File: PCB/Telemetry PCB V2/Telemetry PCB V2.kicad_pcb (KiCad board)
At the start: 4 copper layers, 70 x 70 mm, 50 parts, among them IC1 E22-900M22S, J1 USB_C_Receptacle_USB2.0_16P, J2 DBG/PGRM Hdr., J3 DATA IN, J4 GPS, J5 Batt, SW1 SW_MEC_5E, SW2 SW_MEC_5E, U1 STM32F411CEUx, U2 MCP1700x-250xxTT, U3 AP62200WU, Y1 25MHZ 20pF, Y2 32.768k 12.5pF

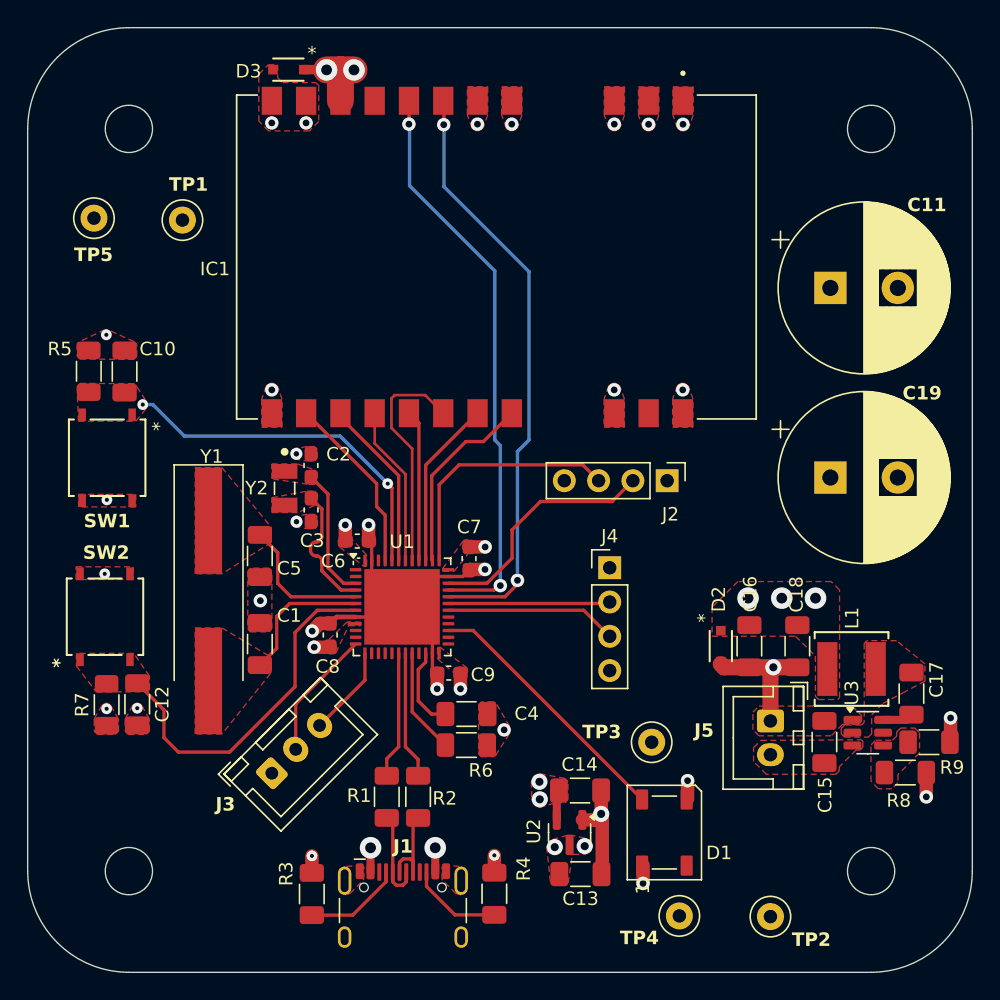
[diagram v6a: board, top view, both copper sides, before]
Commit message: :D
board is done as best I can tell

This update fully removed the smoothing caps as experienced people don't believe they are necessary. This resulted in moving a couple components around.

The vias greater than 0.5mm have had solder mask free zones added on them to prevent JLC from trying plug them because JLC says that plugging is likely to fail on large vias.
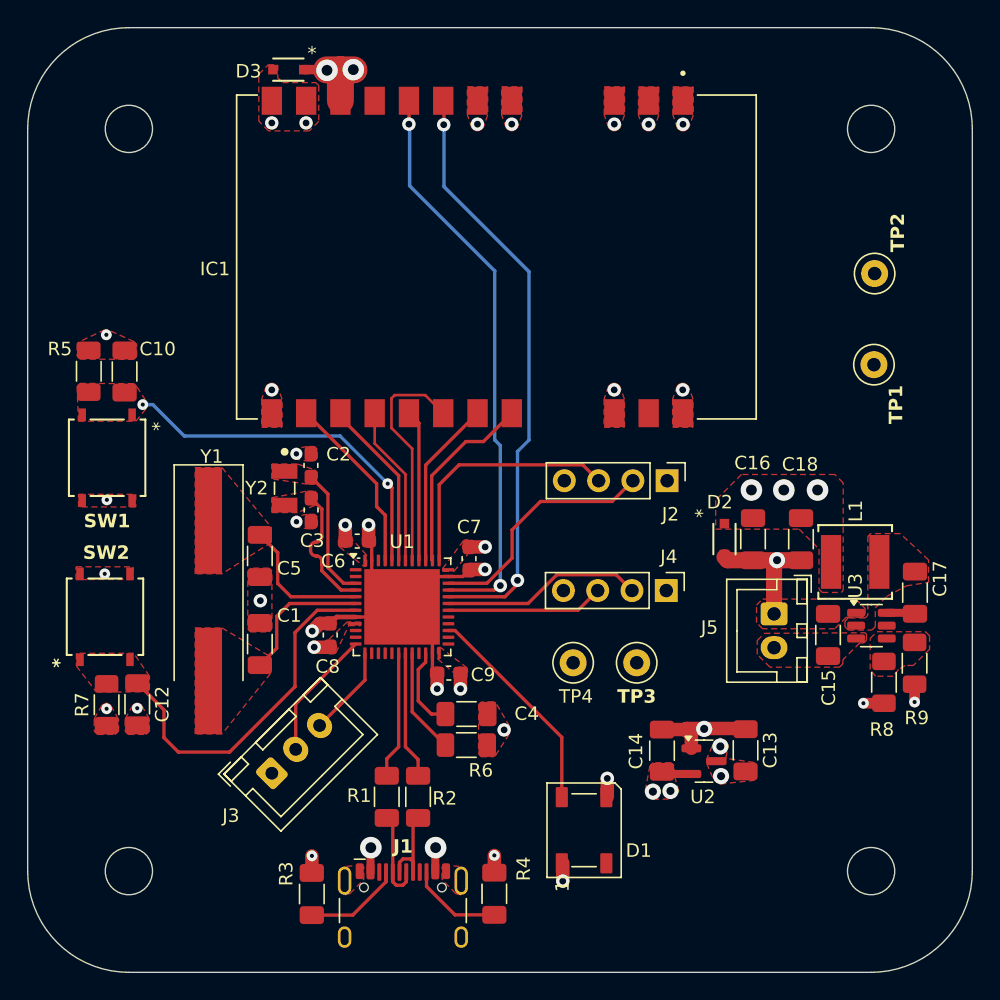
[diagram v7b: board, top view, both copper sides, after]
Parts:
- removed C11, C19: 1000uF, Capacitor_THT:CP_Radial_D12.5mm_P5.00mm
- removed the TP1 at (134.3, 62.7)
- removed TP5: TestPoint, TestPoint:TestPoint_Loop_D1.80mm_Drill1.0mm_Beaded
- added TP4: TestPoint, TestPoint:TestPoint_Loop_D1.80mm_Drill1.0mm_Beaded, F.Cu at (163.3, 95.5)
- J5: value Batt -> Battery
- moved TP2 48.3 mm to (185.6, 66.7), turned to 90 degrees
- moved TP1 43.3 mm to (185.6, 73.4), turned to 90 degrees
- moved C13 15.3 mm to (176.1, 102.0), turned to 90 degrees
- moved U2 11.3 mm to (173.0, 102.8), turned to 0 degrees
- moved C15 7.94 mm to (182.2, 93.4)
- moved C16 7.94 mm to (176.6, 86.3)
- moved C18 7.94 mm to (180.2, 86.3)
- moved L1 7.94 mm to (184.2, 88.0)
- moved U3 7.94 mm to (185.4, 92.7)
- moved D2 7.94 mm to (174.5, 86.3)
- moved J5 7.94 mm to (178.2, 91.9)
- moved C17 7.48 mm to (188.6, 90.3)
- moved R8 6.87 mm to (186.3, 97.0), turned to -90 degrees
- moved C14 6.75 mm to (169.9, 102.0), turned to 90 degrees
- moved TP3 5.99 mm to (168.0, 95.5)
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- renumbered TP4 to TP1
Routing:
- net DIN: track 19.5 -> 16.1 mm
- net RX: track 12.0 -> 15.0 mm
- net TX: track 12.7 -> 11.7 mm
- net +5V: track 13.0 -> 12.4 mm

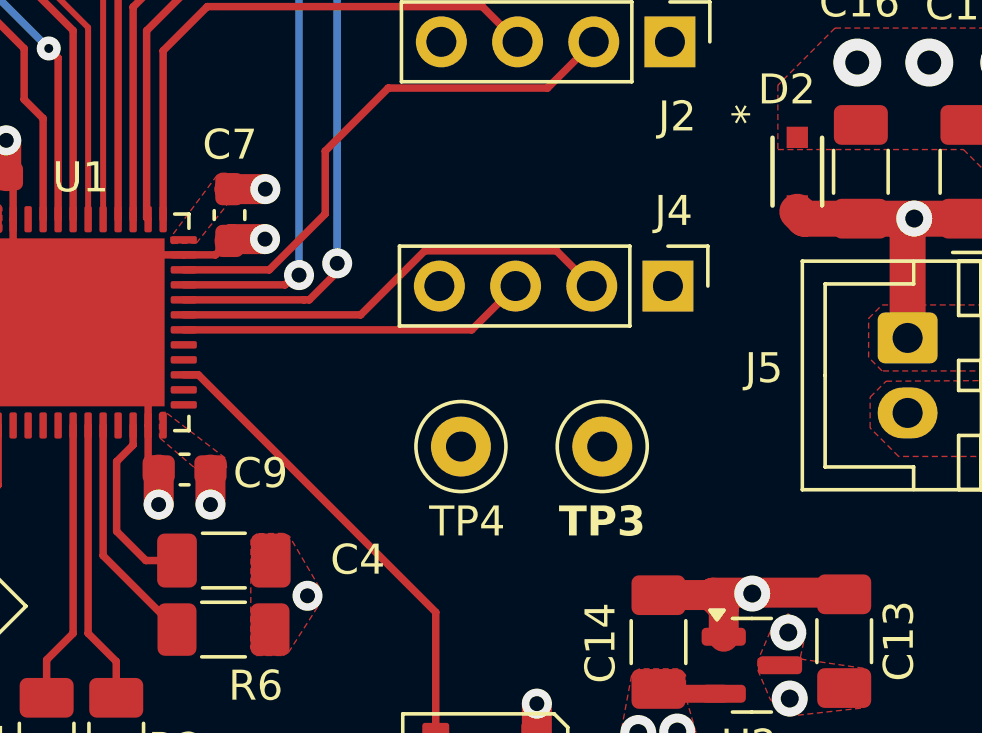
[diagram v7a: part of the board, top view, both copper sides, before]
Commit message: Changed GPS power to 5V
Changed GPS power to 5V because I was not sure what it's current draw is and we don't have a ton of spare capacity on the 3.3V power regulator. Powering of of 5V is also likely more power efficient as it is not passing through a linear voltage regulator
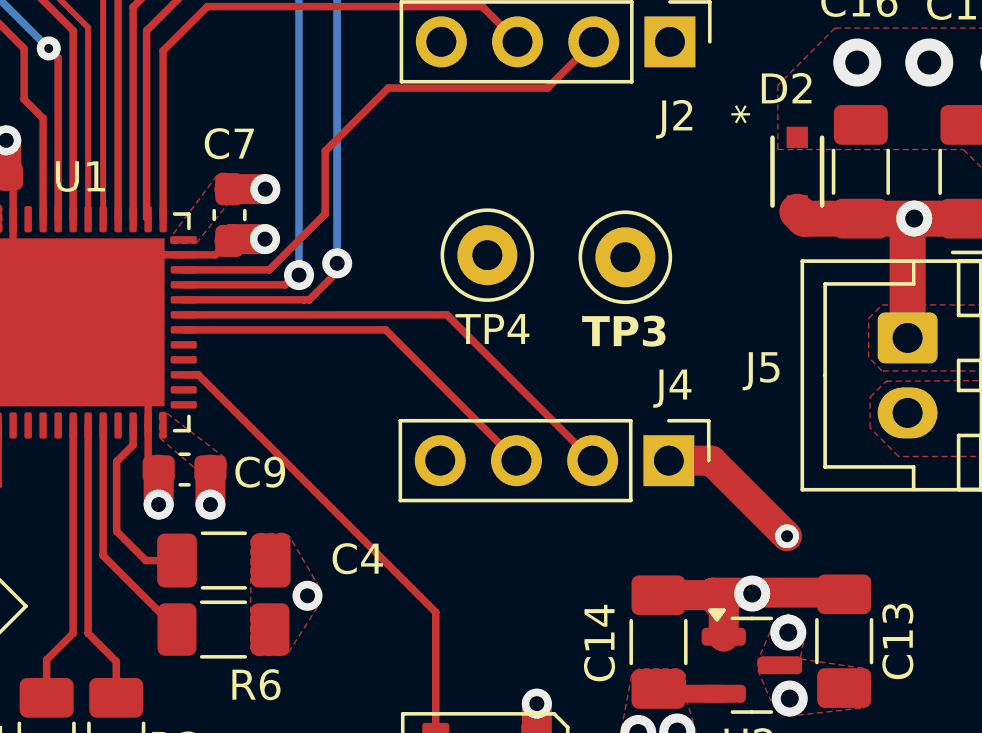
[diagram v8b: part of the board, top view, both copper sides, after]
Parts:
- Y1: value 25MHZ 20pF -> 25MHZ 18pF
- moved TP4 6.44 mm to (164.2, 89.1)
- moved TP3 6.36 mm to (168.8, 89.2)
- moved J4 5.82 mm to (170.2, 96.0)
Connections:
- J4 pad 1: +3.3V -> +5V
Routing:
- net +5V: track 12.4 -> 17.4 mm, vias 11 -> 12
- net TX: track 11.7 -> 12.9 mm
- net RX: track 15.0 -> 15.6 mm
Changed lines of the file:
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@@
 	(footprint "TestPoint:TestPoint_Loop_D1.80mm_Drill1.0mm_Beaded"
 		(layer "F.Cu")
-		(at 168 95.5)
+		(at 168.77 89.19)
 		(descr "wire loop with bead as test point, loop diameter 1.8mm, hole diameter 1.0mm")
 		(tags "test point wire loop bead")
@@
 		(tags "SMD SMT crystal hand-soldering")
 		(property "Reference" "Y1"
-			(at -10.692499 -0.235 180)
+			(at -10.692499 -0.235 360)
 			(layer "F.SilkS")
 			(effects
@@
 			)
 		)
-		(property "Value" "25MHZ 20pF"
+		(property "Value" "25MHZ 18pF"
 			(at -4.322499 3.335 90)
 			(layer "F.Fab")
@@
 	(footprint "Connector_PinHeader_2.54mm:PinHeader_1x04_P2.54mm_Vertical"
 		(layer "F.Cu")
-		(at 170.19 90.15 -90)
+		(at 170.22 95.97 -90)
 		(descr "Through hole straight pin header, 1x04, 2.54mm pitch, single row")
 		(tags "Through hole pin header THT 1x04 2.54mm single row")
@@
 			(layers "*.Cu" "*.Mask")
 			(remove_unused_layers no)
-			(net 7 "+3.3V")
+			(net 10 "+5V")
 			(pinfunction "Pin_1")
 			(pintype "passive")
@@
 	(footprint "TestPoint:TestPoint_Loop_D1.80mm_Drill1.0mm_Beaded"
 		(layer "F.Cu")
-		(at 163.29 95.5)
+		(at 164.17 89.12)
 		(descr "wire loop with bead as test point, loop diameter 1.8mm, hole diameter 1.0mm")
 		(tags "test point wire loop bead")
@@
 	)
 	(segment
+		(start 171.64 95.97)
+		(end 174.16 98.49)
+		(width 1)
+		(layer "F.Cu")
+		(net 10)
+	)
+	(segment
 		(start 153.075 109.215)
 		(end 153.07 109.21)
@@
 	)
 	(segment
+		(start 170.22 95.97)
+		(end 171.64 95.97)
+		(width 1)
+		(layer "F.Cu")
+		(net 10)
+	)
+	(segment
 		(start 145 51.55)
 		(end 145.02 51.57)
@@
 	)
 	(via
+		(at 174.16 98.49)
+		(size 0.8)
+		(drill 0.4)
+		(layers "F.Cu" "B.Cu")
+		(net 10)
+	)
+	(via
 		(at 153.1 109.2)
 		(size 1.6)
@@
 	)
 	(segment
-		(start 163.650001 91.61)
-		(end 165.110001 90.15)
+		(start 160.780001 91.61)
+		(end 165.140001 95.97)
 		(width 0.25)
 		(layer "F.Cu")
@@
 	(segment
 		(start 154.05 91.61)
-		(end 163.650001 91.61)
+		(end 160.780001 91.61)
 		(width 0.25)
 		(layer "F.Cu")
@@
 	(segment
 		(start 154.05 91.11)
-		(end 159.948299 91.11)
+		(end 162.82 91.11)
 		(width 0.25)
 		(layer "F.Cu")
@@
 	)
 	(segment
-		(start 159.948299 91.11)
-		(end 162.083299 88.975)
-		(width 0.25)
-		(layer "F.Cu")
-		(net 29)
-	)
-	(segment
-		(start 166.475 88.975)
-		(end 167.65 90.15)
-		(width 0.25)
-		(layer "F.Cu")
-		(net 29)
-	)
-	(segment
-		(start 162.083299 88.975)
-		(end 166.475 88.975)
+		(start 162.82 91.11)
+		(end 167.68 95.97)
 		(width 0.25)
 		(layer "F.Cu")
@@
 	)
 	(zone
-		(net 9)
-		(net_name "BOOT0")
-		(layer "F.Cu")
-		(name "$teardrop_padvia$")
-		(hatch full 0.1)
-		(priority 30002)
-		(attr
-			(teardrop
-				(type padvia)
-			)
-		)
-		(connect_pads yes
-			(clearance 0)
-		)
-		(min_thickness 0.0254)
-		(filled_areas_thickness no)
-		(fill yes
-			(thermal_gap 0.5)
-			(thermal_bridge_width 0.5)
-			(island_removal_mode 1)
-			(island_area_min 10)
-		)
-		(polygon
-			(pts
-				(xy 149.7375 82.900559) (xy 149.9875 82.900559) (xy 149.95 82.23) (xy 149.55 82.229) (xy 149.267157 82.512843)
-			)
-		)
-	)
-	(zone
 		(net 1)
 		(net_name "GND")
@@
 	)
 	(zone
+		(net 9)
+		(net_name "BOOT0")
+		(layer "F.Cu")
+		(name "$teardrop_padvia$")
+		(hatch full 0.1)
+		(priority 30002)
+		(attr
+			(teardrop
+				(type padvia)
+			)
+		)
+		(connect_pads yes
+			(clearance 0)
+		)
+		(min_thickness 0.0254)
+		(filled_areas_thickness no)
+		(fill yes
+			(thermal_gap 0.5)
+			(thermal_bridge_width 0.5)
+			(island_removal_mode 1)
+			(island_area_min 10)
+		)
+		(polygon
+			(pts
+				(xy 149.7375 82.900559) (xy 149.9875 82.900559) (xy 149.95 82.23) (xy 149.55 82.229) (xy 149.267157 82.512843)
+			)
+		)
+	)
+	(zone
 		(net 7)
 		(net_name "+3.3V")
@@
 	)
 	(zone
-		(net 23)
-		(net_name "TXEN")
-		(layer "F.Cu")
-		(name "$teardrop_padvia$")
-		(hatch full 0.1)
-		(priority 30000)
-		(attr
-			(teardrop
-				(type padvia)
-			)
-		)
-		(connect_pads yes
-			(clearance 0)
-		)
-		(min_thickness 0.0254)
-		(filled_areas_thickness no)
-		(fill yes
-			(thermal_gap 0.5)
-			(thermal_bridge_width 0.5)
-			(island_removal_mode 1)
-			(island_area_min 10)
-		)
-		(polygon
-			(pts
-				(xy 151.255 54.591989) (xy 151.005 54.591989) (xy 150.65806 55.398658) (xy 151.12 55.591) (xy 151.58194 55.398658)
-			)
-		)
-	)
-	(zone
 		(net 20)
 		(net_name "RXEN")
@@
 	)
 	(zone
+		(net 23)
+		(net_name "TXEN")
+		(layer "F.Cu")
+		(name "$teardrop_padvia$")
+		(hatch full 0.1)
+		(priority 30000)
+		(attr
+			(teardrop
+				(type padvia)
+			)
+		)
+		(connect_pads yes
+			(clearance 0)
+		)
+		(min_thickness 0.0254)
+		(filled_areas_thickness no)
+		(fill yes
+			(thermal_gap 0.5)
+			(thermal_bridge_width 0.5)
+			(island_removal_mode 1)
+			(island_area_min 10)
+		)
+		(polygon
+			(pts
+				(xy 151.255 54.591989) (xy 151.005 54.591989) (xy 150.65806 55.398658) (xy 151.12 55.591) (xy 151.58194 55.398658)
+			)
+		)
+	)
+	(zone
 		(net 0)
 		(net_name "")
@@
 	)
 	(zone
-		(net 23)
-		(net_name "TXEN")
+		(net 20)
+		(net_name "RXEN")
 		(layer "B.Cu")
 		(name "$teardrop_padvia$")
 		(hatch full 0.1)
-		(priority 30001)
+		(priority 30000)
 		(attr
 			(teardrop
@@
 		(polygon
 			(pts
-				(xy 151.045 56.580054) (xy 151.295 56.580054) (xy 151.58194 55.781342) (xy 151.12 55.589) (xy 150.65806 55.781342)
+				(xy 153.595 56.626022) (xy 153.845 56.626022) (xy 154.16194 55.821342) (xy 153.7 55.629) (xy 153.23806 55.821342)
 			)
 		)
 	)
 	(zone
-		(net 9)
-		(net_name "BOOT0")
+		(net 23)
+		(net_name "TXEN")
 		(layer "B.Cu")
 		(name "$teardrop_padvia$")
 		(hatch full 0.1)
-		(priority 30003)
+		(priority 30001)
 		(attr
 			(teardrop
@@
 		(polygon
 			(pts
-				(xy 132.096967 76.493743) (xy 132.273743 76.316967) (xy 131.553073 76.000448) (xy 131.399293 76.369293)
-				(xy 131.553073 76.739552)
+				(xy 151.045 56.580054) (xy 151.295 56.580054) (xy 151.58194 55.781342) (xy 151.12 55.589) (xy 150.65806 55.781342)
 			)
 		)
 	)
 	(zone
-		(net 20)
-		(net_name "RXEN")
+		(net 9)
+		(net_name "BOOT0")
 		(layer "B.Cu")
 		(name "$teardrop_padvia$")
 		(hatch full 0.1)
-		(priority 30000)
+		(priority 30003)
 		(attr
 			(teardrop
@@
 		(polygon
 			(pts
-				(xy 153.595 56.626022) (xy 153.845 56.626022) (xy 154.16194 55.821342) (xy 153.7 55.629) (xy 153.23806 55.821342)
+				(xy 132.096967 76.493743) (xy 132.273743 76.316967) (xy 131.553073 76.000448) (xy 131.399293 76.369293)
+				(xy 131.553073 76.739552)
 			)
 		)
